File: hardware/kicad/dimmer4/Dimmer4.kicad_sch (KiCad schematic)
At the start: 41 parts, among them J100 Stapelstecker 2x20, J101 Kettenstecker, Buchse oben (S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, J102 Kettenstecker, Stift unten (S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, J103 Leistungsstecker, Buchse oben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, J104 Leistungsstecker, Stift unten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, J5 LED-Kanal 1, J6 LED-Kanal 2, J7 LED-Kanal 3, J8 LED-Kanal 4, Q1 NCE6050KA, Q10 IRFR5305, Q2 NCE6050KA, Q3 NCE6050KA, Q4 NCE6050KA, U100 STM32C011F6P6, U101 SN74LVC1G175, U102 SN74LVC2G00DCUR, U103 SN74LVC1G08

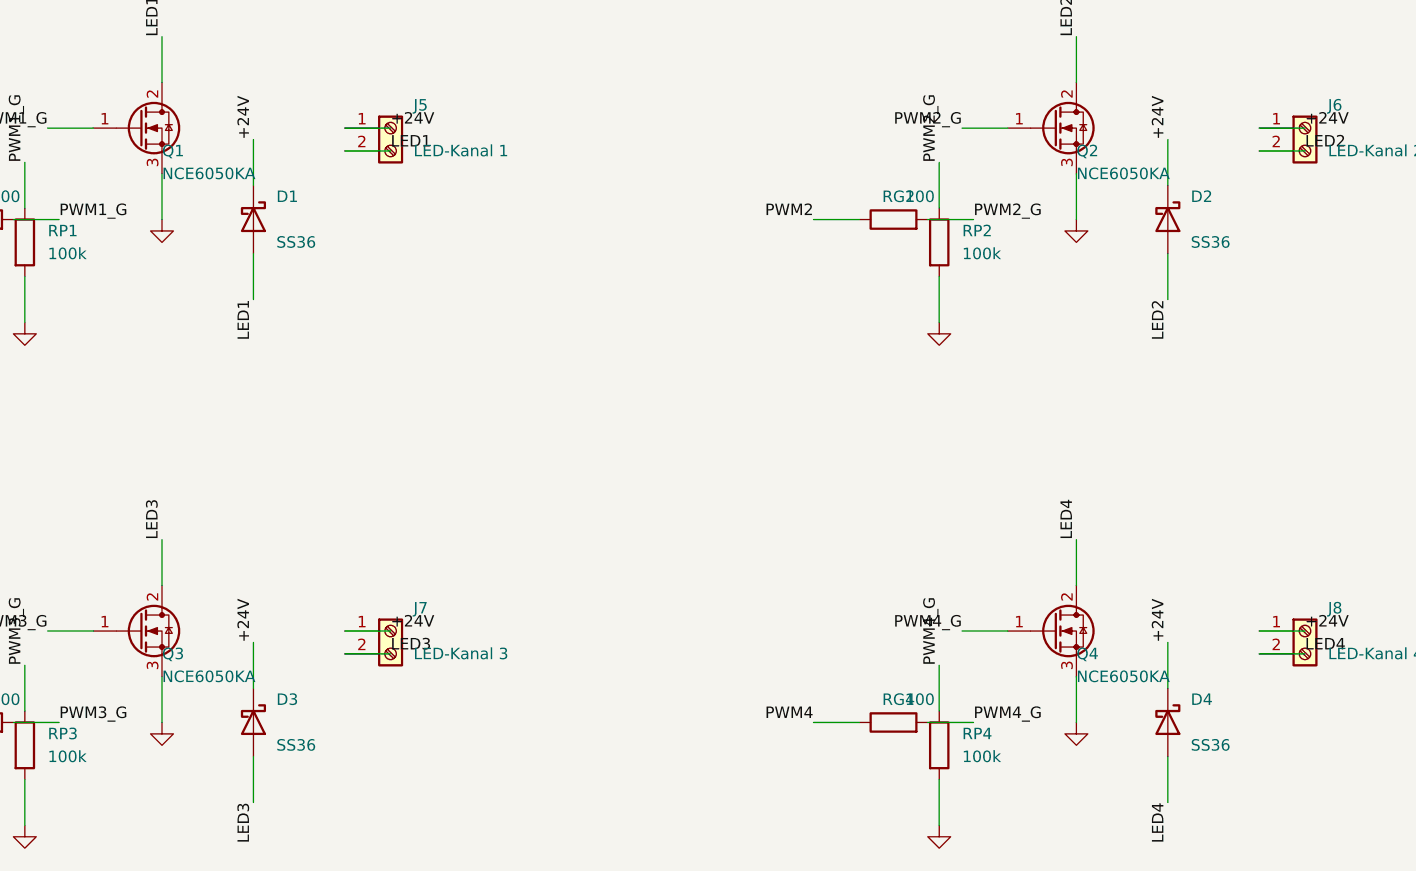
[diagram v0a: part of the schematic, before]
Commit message: Lager-Runde 2: NCE6020AK statt 6050KA, Basic-Widerstaende, Belege
JLCs zweiter Abgleich zeigte: NCE6050KA ausverkauft (3 Stueck Rest),
drei Widerstands-Matches auf Lager-0-Teile. Kanal-FET auf NCE6020AK
(C108639) umgestellt -- gleiches VGS(th)-Limit, Rechnung und ehrlicher
Vorbehalt in dimmermodul.py; Kennwiderstaende kriegen ihre Nummern
jetzt wertbasiert aus LCSC_KENN. Alle neuen Nummern an der
LCSC-Produktseite gesichtet (hardware/bauteile-dimmer.md, Nachtrag).
Dimmer-Schaltplaene regeneriert (ERC 0/0), 12 Suiten gruen.

Co-Authored-By: Claude Fable 5 <noreply@anthropic.com>
Claude-Session: https://claude.ai/code/session_01KDus95JJwCeRuwccgBWEi5
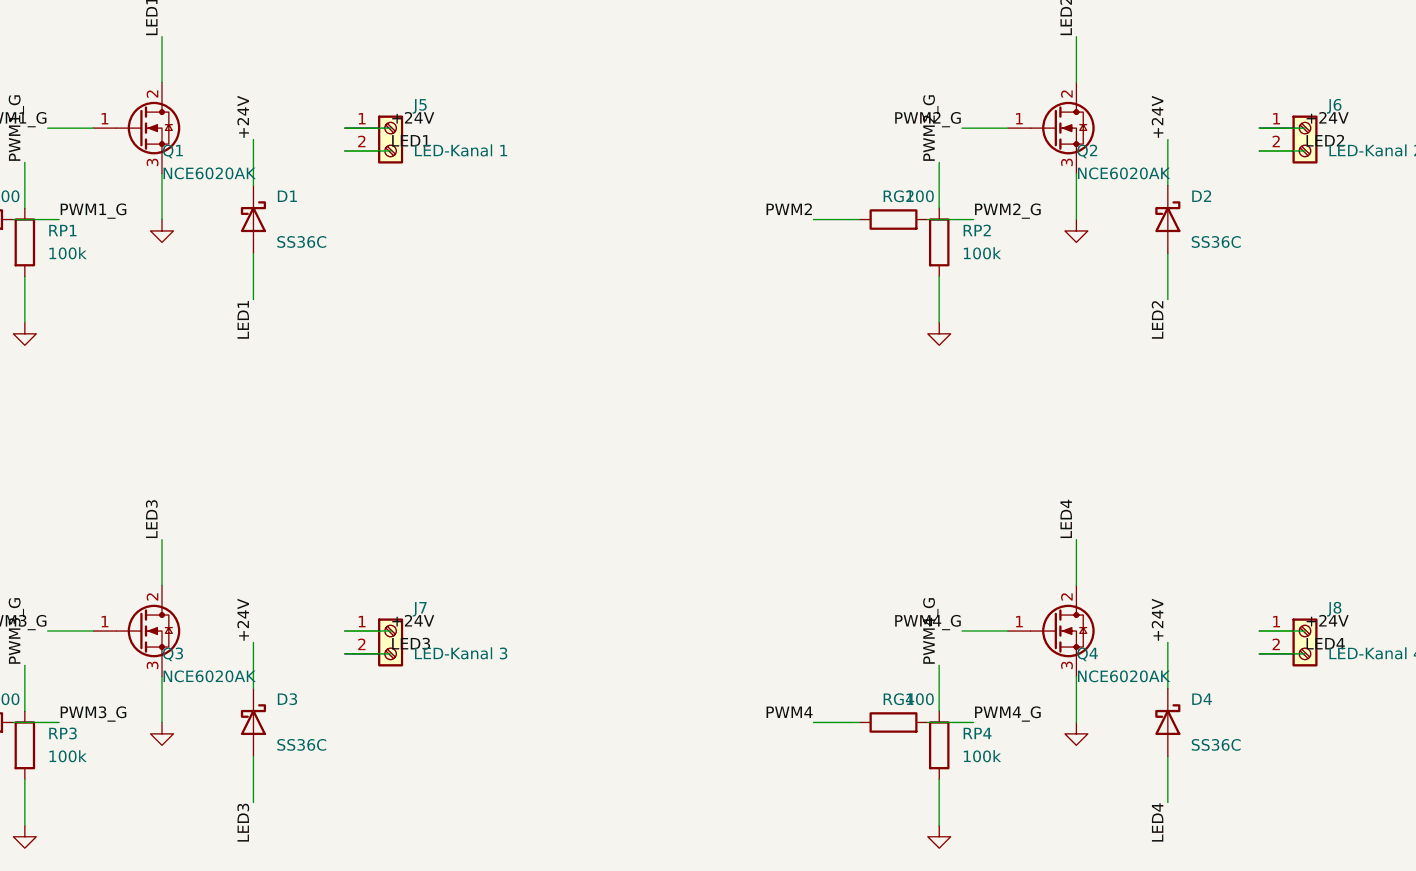
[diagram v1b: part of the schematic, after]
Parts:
- D1, D2, D3, D4: value SS36 -> SS36C
- Q1, Q2, Q3, Q4: value NCE6050KA -> NCE6020AK

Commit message: Dimmermodul v2: Versorgungszelle statt Q10-Strang, Gatter-Abblockung, v2-Scaffold
Ersetzt den alten Q10/R11/R12/D10/C12-Verpolschutzstrang durch
versorgung.bauen() (Task 3/5-Zelle, richtig gepolt) mit eigener
Einspeiseklemme J90; ergaenzt Abblockkondensatoren fuer U101/U102/U103
(bislang unversorgt) und die v2-Randpad-Kante (frei_durchreichen=True
+ randpads()) nach dem Motormodul-Muster.

PWM_PINS bleibt bewusst UNVERAENDERT: die vom Aufgabenbrief
vorgeschlagene Verlegung von Kanal 3/4 auf PA5/PA6 (Pin 12/13) ist
nicht moeglich, weil modulsockel.py diese Pins fuer JEDES Modul mit
mit_flipflop=True unbedingt auf NFAULT/IPROPI verdrahtet (verifiziert
am STM32C011-Symbol UND am Code) -- ueber die Kanal-1/2-Pins PA8/PA7
hinaus gibt es keinen einzigen freien Port-A-Pin. Volle Herleitung im
Docstring und in task-6-report.md.

ERC (severity-error) exit 0 fuer Dimmer1/3/4; Rot-Liste von
tests/run_all.py unveraendert (5 vorbestehende, unabhaengige
Fehlschlaege in sockelplatine.py/spec_sockel.py).

Co-Authored-By: Claude Fable 5 <noreply@anthropic.com>
Claude-Session: https://claude.ai/code/session_01KDus95JJwCeRuwccgBWEi5
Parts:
- removed C12: 220u, Capacitor_THT:CP_Radial_D8.0mm_P3.50mm, symbol Device:C_Polarized
- removed D10: SMCJ30A, Diode_SMD:D_SMC, symbol Device:D_Zener
- removed J100: Stapelstecker 2x20, Connector_PinHeader_2.54mm:PinHeader_2x20_P2.54mm_Vertical, symbol Connector_Generic:Conn_02x20_Odd_Even
- removed Q10: IRFR5305, Package_TO_SOT_SMD:TO-252-3_TabPin2, symbol Transistor_FET:Q_PMOS_GDS
- removed R11, R12: 10k, Resistor_SMD:R_0805_2012Metric_Pad1.20x1.40mm_HandSolder, symbol Device:R
- added C102, C103, C104: 100n, Capacitor_SMD:C_0805_2012Metric_Pad1.18x1.45mm_HandSolder, symbol Device:C
- added C90: 220u, Capacitor_THT:CP_Radial_D8.0mm_P3.50mm, symbol Device:C_Polarized
- added C91: 22u, Capacitor_SMD:C_0805_2012Metric_Pad1.18x1.45mm_HandSolder, symbol Device:C
- added D90: SMCJ30A, Diode_SMD:D_SMC, symbol Device:D_Zener
- added D91: SS36C, Diode_SMD:D_SMC, symbol Device:D_Schottky
- added J100: Stapelstecker links, Pico-Pins 1..20 (Buchse), Connector_PinSocket_2.54mm:PinSocket_1x20_P2.54mm_Vertical, symbol Connector_Generic:Conn_01x20
- added J105: Stapelstecker rechts, Pico-Pins 21..40 (Buchse), Connector_PinSocket_2.54mm:PinSocket_1x20_P2.54mm_Vertical, symbol Connector_Generic:Conn_01x20
- added J90: Versorgung Eingang, TerminalBlock_Phoenix:TerminalBlock_Phoenix_PT-1,5-2-3.5-H_1x02_P3.50mm_Horizontal, symbol Connector:Screw_Terminal_01x02
- added J95: Randpads GPIO, unbestueckt (THT-Loetpad), Connector_PinHeader_2.54mm:PinHeader_1x18_P2.54mm_Vertical, symbol Connector_Generic:Conn_01x18
- added J96: Randpads Versorgung: 2x 3V3 + 2x GND, unbestueckt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, Connector_PinHeader_2.54mm:PinHeader_1x04_P2.54mm_Vertical, symbol Connector_Generic:Conn_01x04
- added Q90: IRFR5305, Package_TO_SOT_SMD:TO-252-3_TabPin2, symbol Transistor_FET:Q_PMOS_GDS
- added R90, R91: 10k, Resistor_SMD:R_0805_2012Metric_Pad1.20x1.40mm_HandSolder, symbol Device:R
- added U90: K7805-1000R3, Converter_DCDC:Converter_DCDC_RECOM_R-78B-2.0_THT, symbol Converter_DCDC:R-78B5.0-2.0
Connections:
- net PWR24V is gone; now on net +24V: J103.1 (Pin_1), J103.3 (Pin_3), J104.1 (Pin_1), J104.3 (Pin_3)
- net +24V: now also C90.1, D90.1 (K), Q90.3 (S), R90.2, U90.1 (IN)
- net 3V3: now also C102.1, C102.2, C103.1, C103.2, C104.1, C104.2, C90.2, C91.2, D90.2 (A), J100.13 (Pin_13), J100.18 (Pin_18), J100.3 (Pin_3), J100.8 (Pin_8), J105.13 (Pin_13), J105.16 (Pin_16), J105.18 (Pin_18), J105.3 (Pin_3), J105.8 (Pin_8), J90.2 (Pin_2), J96.1 (Pin_1), J96.2 (Pin_2), J96.3 (Pin_3), J96.4 (Pin_4), R91.2, U90.2 (GND)
- net FLASH_MODE: now also J100.5 (Pin_5)
- net FLASH_RX: now also J100.2 (Pin_2)
- net FLASH_TX: now also J100.1 (Pin_1)
- net I2C_SCL: now also J100.7 (Pin_7)
- net I2C_SDA: now also J100.6 (Pin_6)
- net NOTAUS: now also J100.9 (Pin_9)
- net SEL_CLK: now also J100.10 (Pin_10)
- new net +5V_LOKAL: C91.1, D91.2 (A), U90.3 (OUT)
- new net GP10: J100.14 (Pin_14), J95.3 (Pin_3)
- new net GP11: J100.15 (Pin_15), J95.4 (Pin_4)
- new net GP12: J100.16 (Pin_16), J95.5 (Pin_5)
- new net GP13: J100.17 (Pin_17), J95.6 (Pin_6)
- new net GP14: J100.19 (Pin_19), J95.7 (Pin_7)
- new net GP15: J100.20 (Pin_20), J95.8 (Pin_8)
- new net GP16: J105.1 (Pin_1), J95.9 (Pin_9)
- new net GP17: J105.2 (Pin_2), J95.10 (Pin_10)
- new net GP18: J105.4 (Pin_4), J95.11 (Pin_11)
- new net GP19: J105.5 (Pin_5), J95.12 (Pin_12)
- new net GP20: J105.6 (Pin_6), J95.13 (Pin_13)
- new net GP21: J105.7 (Pin_7), J95.14 (Pin_14)
- new net GP22: J105.9 (Pin_9), J95.15 (Pin_15)
- new net GP26: J105.11 (Pin_11), J95.16 (Pin_16)
- new net GP27: J105.12 (Pin_12), J95.17 (Pin_17)
- new net GP28: J105.14 (Pin_14), J95.18 (Pin_18)
- new net GP8: J100.11 (Pin_11), J95.1 (Pin_1)
- new net GP9: J100.12 (Pin_12), J95.2 (Pin_2)
- new net PWR_IN: J90.1 (Pin_1), Q90.2 (D)
- new net Q90_GATE: Q90.1 (G), R90.1, R91.1
- new net VSYS: D91.1 (K), J105.19 (Pin_19)
- no-connect marks 25 -> 6

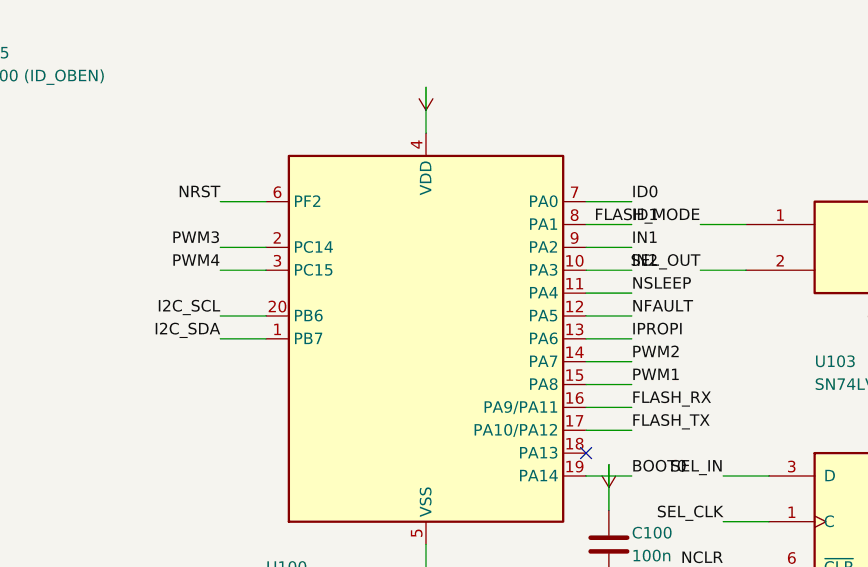
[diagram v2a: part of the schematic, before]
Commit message: Fix-Runde 1 zu Task 6: Motorsignale optional, PWM3/4 auf PA5/PA6
modulsockel.einbauen() verdrahtete PA2..PA6 (Pin 9-13) bisher
UNBEDINGT auf die DRV8876-Motorsignale (IN1/IN2/NSLEEP/NFAULT/IPROPI)
-- eine Altlast aus der Zeit mit nur einem Modultyp, die jedem Modul
ohne eigenen Motortreiber fuenf Port-A-Pins kostete. Neuer Parameter
motorsignale=False (Vorgabe): nur ein Modul mit motorsignale=True
(Motormodul) bekommt die feste Verdrahtung, jedes andere Modul
behandelt die fuenf Pins wie gewoehnliche freie GPIO (zusatz_pins oder
no_connect).

Motormodul fordert die Signale jetzt explizit an (motorsignale=True) --
Regressionsnachweis: generierte Netzliste vor/nach dem Umbau
byte-identisch (Schaltplan-Diff und Netlist-Export je UUID-/Datum-
normalisiert verglichen), ERC unveraendert 0 Fehler/2 Warnungen.

Dimmermodul: PWM3/4 ziehen von den schwach treibenden OSC32-Pins
PC14/PC15 auf PA5/PA6 (Pin 12/13) um -- damit haben jetzt alle vier
Kanaele Port-A-Pins mit Timer-Faehigkeit. tests/test_modulsockel.py
angepasst (Erwartungswert + drei neue Gegenproben fuer das neue
motorsignale-Verhalten, inkl. Kollisions-ValueError).

ERC (severity-error) exit 0 fuer Motormodul + Dimmer1/3/4; Rot-Liste
von tests/run_all.py unveraendert bei den 5 vorbestehenden,
unabhaengigen Fehlschlaegen.

Co-Authored-By: Claude Fable 5 <noreply@anthropic.com>
Claude-Session: https://claude.ai/code/session_01KDus95JJwCeRuwccgBWEi5
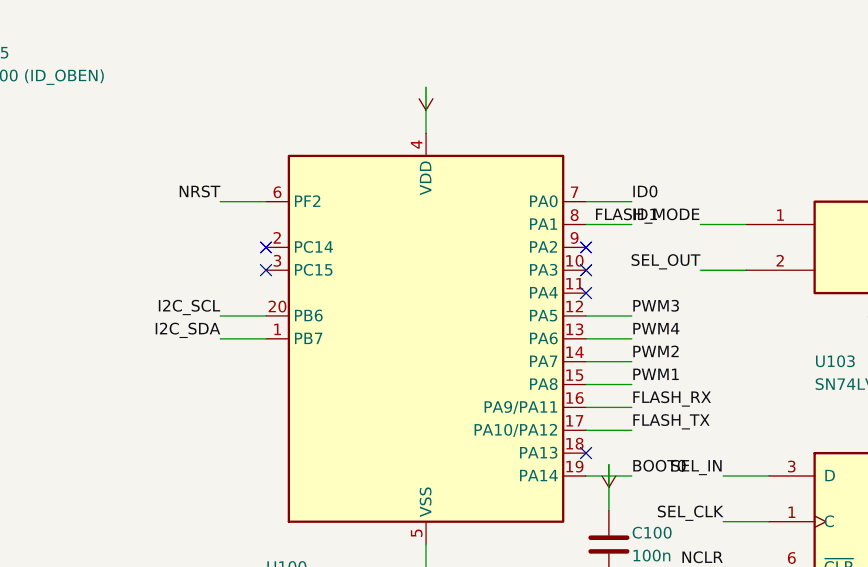
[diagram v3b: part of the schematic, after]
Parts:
- removed C102: 100n, Capacitor_SMD:C_0805_2012Metric_Pad1.18x1.45mm_HandSolder, symbol Device:C
- removed D4: SS36C, Diode_SMD:D_SMC, symbol Device:D_Schottky
- removed J8: LED-Kanal 4, TerminalBlock_Phoenix:TerminalBlock_Phoenix_PT-1,5-2-3.5-H_1x02_P3.50mm_Horizontal, symbol Connector:Screw_Terminal_01x02
- removed J95: Randpads GPIO, unbestueckt (THT-Loetpad), Connector_PinHeader_2.54mm:PinHeader_1x18_P2.54mm_Vertical, symbol Connector_Generic:Conn_01x18
- removed Q4: NCE6020AK, Package_TO_SOT_SMD:TO-252-3_TabPin2, symbol Transistor_FET:Q_NMOS_GDS
- removed RG4: 100, Resistor_SMD:R_0805_2012Metric_Pad1.20x1.40mm_HandSolder, symbol Device:R
- removed RP4: 100k, Resistor_SMD:R_0805_2012Metric_Pad1.20x1.40mm_HandSolder, symbol Device:R
- added C90: 220u, Capacitor_THT:CP_Radial_D8.0mm_P3.50mm, symbol Device:C_Polarized
- added J100: Stapelstecker links, Pico-Pins 1..20 (Buchse), Connector_PinSocket_2.54mm:PinSocket_1x20_P2.54mm_Vertical, symbol Connector_Generic:Conn_01x20
- added J101: Kettenstecker, Buchse oben (SMD), Connector_PinSocket_2.54mm:PinSocket_1x02_P2.54mm_Vertical_SMD_Pin1Left, symbol Connector_Generic:Conn_01x02
- added J102: Kettenstecker, Stift unten (SMD), Connector_PinHeader_2.54mm:PinHeader_1x02_P2.54mm_Vertical_SMD_Pin1Left, symbol Connector_Generic:Conn_01x02
- added J103: Leistungsstecker, Buchse oben (SMD), Connector_PinSocket_2.54mm:PinSocket_2x02_P2.54mm_Vertical_SMD, symbol Connector_Generic:Conn_02x02_Odd_Even
- added J105: Stapelstecker rechts, Pico-Pins 21..40 (Buchse), Connector_PinSocket_2.54mm:PinSocket_1x20_P2.54mm_Vertical, symbol Connector_Generic:Conn_01x20
- added R91: 10k, Resistor_SMD:R_0805_2012Metric_Pad1.20x1.40mm_HandSolder, symbol Device:R
- C100: renamed from J101; value Kettenstecker, Buchse oben (SMD) -> 100n; footprint Connector_PinSocket_2.54mm:PinSocket_1x02_P2.54mm_Vertical_SMD_Pin1Left -> Capacitor_SMD:C_0805_2012Metric_Pad1.18x1.45mm_HandSolder; symbol Connector_Generic:Conn_01x02 -> Device:C
- C101: renamed from J104; value Leistungsstecker, Stift unten (SMD) -> 1000n; footprint Connector_PinHeader_2.54mm:PinHeader_2x02_P2.54mm_Vertical_SMD -> Capacitor_SMD:C_0805_2012Metric_Pad1.18x1.45mm_HandSolder; symbol Connector_Generic:Conn_02x02_Odd_Even -> Device:C
- C102: renamed from R100; value Kennwiderstand (Modultyp) -> 100n; footprint Resistor_SMD:R_0805_2012Metric_Pad1.20x1.40mm_HandSolder -> Capacitor_SMD:C_0805_2012Metric_Pad1.18x1.45mm_HandSolder; symbol Device:R -> Device:C; LCSC (none) -> C49678
- C103: renamed from R105; value 10000 (ID_OBEN) -> 100n; footprint Resistor_SMD:R_0805_2012Metric_Pad1.20x1.40mm_HandSolder -> Capacitor_SMD:C_0805_2012Metric_Pad1.18x1.45mm_HandSolder; symbol Device:R -> Device:C; LCSC (none) -> C49678
- C104: renamed from R101; value Kennwiderstand (Modultyp) -> 100n; footprint Resistor_SMD:R_0805_2012Metric_Pad1.20x1.40mm_HandSolder -> Capacitor_SMD:C_0805_2012Metric_Pad1.18x1.45mm_HandSolder; symbol Device:R -> Device:C; LCSC (none) -> C49678
- C91: renamed from R90; value 10k -> 22u; footprint Resistor_SMD:R_0805_2012Metric_Pad1.20x1.40mm_HandSolder -> Capacitor_SMD:C_0805_2012Metric_Pad1.18x1.45mm_HandSolder; symbol Device:R -> Device:C
- D1: renamed from C91; value 22u -> SS36C; footprint Capacitor_SMD:C_0805_2012Metric_Pad1.18x1.45mm_HandSolder -> Diode_SMD:D_SMC; symbol Device:C -> Device:D_Schottky
- D90: renamed from J90; value Versorgung Eingang -> SMCJ30A; footprint TerminalBlock_Phoenix:TerminalBlock_Phoenix_PT-1,5-2-3.5-H_1x02_P3.50mm_Horizontal -> Diode_SMD:D_SMC; symbol Connector:Screw_Terminal_01x02 -> Device:D_Zener
- D91: renamed from R91; value 10k -> SS36C; footprint Resistor_SMD:R_0805_2012Metric_Pad1.20x1.40mm_HandSolder -> Diode_SMD:D_SMC; symbol Device:R -> Device:D_Schottky
- J104: renamed from J100; value Stapelstecker links, Pico-Pins 1..20 (Buchse) -> Leistungsstecker, Stift unten (SMD); footprint Connector_PinSocket_2.54mm:PinSocket_1x20_P2.54mm_Vertical -> Connector_PinHeader_2.54mm:PinHeader_2x02_P2.54mm_Vertical_SMD; symbol Connector_Generic:Conn_01x20 -> Connector_Generic:Conn_02x02_Odd_Even
- J5: renamed from D91; value SS36C -> LED-Kanal 1; footprint Diode_SMD:D_SMC -> TerminalBlock_Phoenix:TerminalBlock_Phoenix_PT-1,5-2-3.5-H_1x02_P3.50mm_Horizontal; symbol Device:D_Schottky -> Connector:Screw_Terminal_01x02
- J6: renamed from J5; value LED-Kanal 1 -> LED-Kanal 2
- J7: renamed from J6; value LED-Kanal 2 -> LED-Kanal 3
- J8: renamed from J7; value LED-Kanal 3 -> LED-Kanal 4
- J90: renamed from J96; value Randpads Versorgung: 2x 3V3 + 2x GND, unbestueckt (THT-Loetpad) -> Versorgung Eingang; footprint Connector_PinHeader_2.54mm:PinHeader_1x04_P2.54mm_Vertical -> TerminalBlock_Phoenix:TerminalBlock_Phoenix_PT-1,5-2-3.5-H_1x02_P3.50mm_Horizontal; symbol Connector_Generic:Conn_01x04 -> Connector:Screw_Terminal_01x02; now fitted
- J95: renamed from U103; value SN74LVC1G08 -> Randpads GPIO, unbestueckt (THT-Loetpad); footprint Package_TO_SOT_SMD:SOT-353_SC-70-5 -> Connector_PinHeader_2.54mm:PinHeader_1x18_P2.54mm_Vertical; symbol 74xGxx:74LVC1G08 -> Connector_Generic:Conn_01x18; now not fitted
- J96: renamed from R104; value 10000 (ID_OBEN) -> Randpads Versorgung: 2x 3V3 + 2x GND, unbestueckt (THT-Loetpad); footprint Resistor_SMD:R_0805_2012Metric_Pad1.20x1.40mm_HandSolder -> Connector_PinHeader_2.54mm:PinHeader_1x04_P2.54mm_Vertical; symbol Device:R -> Connector_Generic:Conn_01x04; now not fitted
- Q1: renamed from D90; value SMCJ30A -> NCE6020AK; footprint Diode_SMD:D_SMC -> Package_TO_SOT_SMD:TO-252-3_TabPin2; symbol Device:D_Zener -> Transistor_FET:Q_NMOS_GDS
- Q90: renamed from C103; value 100n -> IRFR5305; footprint Capacitor_SMD:C_0805_2012Metric_Pad1.18x1.45mm_HandSolder -> Package_TO_SOT_SMD:TO-252-3_TabPin2; symbol Device:C -> Transistor_FET:Q_PMOS_GDS; LCSC C49678 -> (none)
- R100, R101: renamed from U102; value SN74LVC2G00DCUR -> Kennwiderstand (Modultyp); footprint Package_SO:VSSOP-8_2.3x2mm_P0.5mm -> Resistor_SMD:R_0805_2012Metric_Pad1.20x1.40mm_HandSolder; symbol 74xGxx:74LVC2G00 -> Device:R
- R102: renamed from J103; value Leistungsstecker, Buchse oben (SMD) -> 100k; footprint Connector_PinSocket_2.54mm:PinSocket_2x02_P2.54mm_Vertical_SMD -> Resistor_SMD:R_0805_2012Metric_Pad1.20x1.40mm_HandSolder; symbol Connector_Generic:Conn_02x02_Odd_Even -> Device:R
- R104: renamed from C101; value 1000n -> 10000 (ID_OBEN); footprint Capacitor_SMD:C_0805_2012Metric_Pad1.18x1.45mm_HandSolder -> Resistor_SMD:R_0805_2012Metric_Pad1.20x1.40mm_HandSolder; symbol Device:C -> Device:R
- R105: renamed from U102; value SN74LVC2G00DCUR -> 10000 (ID_OBEN); footprint Package_SO:VSSOP-8_2.3x2mm_P0.5mm -> Resistor_SMD:R_0805_2012Metric_Pad1.20x1.40mm_HandSolder; symbol 74xGxx:74LVC2G00 -> Device:R
- R90: renamed from C104; value 100n -> 10k; footprint Capacitor_SMD:C_0805_2012Metric_Pad1.18x1.45mm_HandSolder -> Resistor_SMD:R_0805_2012Metric_Pad1.20x1.40mm_HandSolder; symbol Device:C -> Device:R; LCSC C49678 -> (none)
- RG1: renamed from C90; value 220u -> 100; footprint Capacitor_THT:CP_Radial_D8.0mm_P3.50mm -> Resistor_SMD:R_0805_2012Metric_Pad1.20x1.40mm_HandSolder; symbol Device:C_Polarized -> Device:R
- RP1: renamed from U90; value K7805-1000R3 -> 100k; footprint Converter_DCDC:Converter_DCDC_RECOM_R-78B-2.0_THT -> Resistor_SMD:R_0805_2012Metric_Pad1.20x1.40mm_HandSolder; symbol Converter_DCDC:R-78B5.0-2.0 -> Device:R
- U100: renamed from J105; value Stapelstecker rechts, Pico-Pins 21..40 (Buchse) -> STM32C011F6P6; footprint Connector_PinSocket_2.54mm:PinSocket_1x20_P2.54mm_Vertical -> Package_SO:TSSOP-20_4.4x6.5mm_P0.65mm; symbol Connector_Generic:Conn_01x20 -> MCU_ST_STM32C0:STM32C011F6Px
- U101: renamed from J102; value Kettenstecker, Stift unten (SMD) -> SN74LVC1G175; footprint Connector_PinHeader_2.54mm:PinHeader_1x02_P2.54mm_Vertical_SMD_Pin1Left -> Package_TO_SOT_SMD:SOT-363_SC-70-6; symbol Connector_Generic:Conn_01x02 -> 74xGxx:74LVC1G175
- U102: renamed from U100; value STM32C011F6P6 -> SN74LVC2G00DCUR; footprint Package_SO:TSSOP-20_4.4x6.5mm_P0.65mm -> Package_SO:VSSOP-8_2.3x2mm_P0.5mm; symbol MCU_ST_STM32C0:STM32C011F6Px -> 74xGxx:74LVC2G00
- U102: renamed from C100; value 100n -> SN74LVC2G00DCUR; footprint Capacitor_SMD:C_0805_2012Metric_Pad1.18x1.45mm_HandSolder -> Package_SO:VSSOP-8_2.3x2mm_P0.5mm; symbol Device:C -> 74xGxx:74LVC2G00
- U102: renamed from U101; value SN74LVC1G175 -> SN74LVC2G00DCUR; footprint Package_TO_SOT_SMD:SOT-363_SC-70-6 -> Package_SO:VSSOP-8_2.3x2mm_P0.5mm; symbol 74xGxx:74LVC1G175 -> 74xGxx:74LVC2G00
- U103: renamed from R102; value 100k -> SN74LVC1G08; footprint Resistor_SMD:R_0805_2012Metric_Pad1.20x1.40mm_HandSolder -> Package_TO_SOT_SMD:SOT-353_SC-70-5; symbol Device:R -> 74xGxx:74LVC1G08
- U90: renamed from Q90; value IRFR5305 -> K7805-1000R3; footprint Package_TO_SOT_SMD:TO-252-3_TabPin2 -> Converter_DCDC:Converter_DCDC_RECOM_R-78B-2.0_THT; symbol Transistor_FET:Q_PMOS_GDS -> Converter_DCDC:R-78B5.0-2.0
- renumbered D1 to D2, D2 to D3, D3 to D4, Q1 to Q2, Q2 to Q3, Q3 to Q4, RG1 to RG2, RG2 to RG3, RG3 to RG4, RP1 to RP2, RP2 to RP3, RP3 to RP4
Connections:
- net +24V: now also D1.1 (K), D90.1 (K), J104.1 (Pin_1), J104.3 (Pin_3), J5.1 (Pin_1), Q90.3 (S), R90.2, U90.1 (IN), C90.1, J103.1 (Pin_1), J103.3 (Pin_3); no longer C101.1 (Pin_1), C101.3 (Pin_3), C91.2, Q1.1 (K), R102.1 (Pin_1), R102.3 (Pin_3), RG1.1, RP1.1 (IN), U90.3 (S)
- net +5V_LOKAL: now also C91.1, D91.2 (A), U90.3 (OUT); no longer D1.1, J5.2 (A), RP1.3 (OUT)
- net 3V3: now also C100.1, C102.1, C103.2, C104.1, C91.2, J104.2 (Pin_2), J104.4 (Pin_4), J96.2 (Pin_2), J96.3 (Pin_3), J96.4 (Pin_4), Q1.3 (S), R100.2, R101.2, R102.1, R104.1, R105.1, U100.4 (VDD), U100.5 (VSS), U101.5 (VCC), U102.4 (GND), U102.8 (VCC), U103.3 (GND), U103.5 (VCC), U90.2 (GND), C90.2, J100.13 (Pin_13), J100.18 (Pin_18), J100.3 (Pin_3), J100.8 (Pin_8), J101.2 (Pin_2), J102.2 (Pin_2), J103.2 (Pin_2), J103.4 (Pin_4), J105.13 (Pin_13), J105.16 (Pin_16), J105.18 (Pin_18), J105.3 (Pin_3), J105.8 (Pin_8), R91.2; no longer C101.4 (Pin_4), D1.2, D91.2, J104.13 (Pin_13), J104.18 (Pin_18), J104.3 (Pin_3), J104.8 (Pin_8), J90.1 (Pin_1), J90.3 (Pin_3), J90.4 (Pin_4), J95.3 (GND), J95.5 (VCC), Q1.2 (A), Q90.1, Q90.2, R101.4 (GND), R101.8 (VCC), R102.2 (Pin_2), R102.4 (Pin_4), R104.2, R90.1, R90.2, RG1.2, U100.13 (Pin_13), U100.16 (Pin_16), U100.18 (Pin_18), U100.3 (Pin_3), U100.8 (Pin_8), U102.1, U102.2, U102.2 (GND), U102.4 (VDD), U102.5 (VCC), U102.5 (VSS), U103.1
- net BOOT0: now also U100.19 (PA14), U103.4; no longer J95.4, U102.19 (PA14)
- net FLASH_MODE: now also U102.5, U103.1, J100.5 (Pin_5); no longer J104.5 (Pin_5), J95.1, R105.5
- net FLASH_RX: now also U100.16 (PA9/PA11), J100.2 (Pin_2); no longer J104.2 (Pin_2), U102.16 (PA9/PA11)
- net FLASH_TX: now also U100.17 (PA10/PA12), J100.1 (Pin_1); no longer J104.1 (Pin_1), U102.17 (PA10/PA12)
- net GP10: now also J95.3 (Pin_3), J100.14 (Pin_14); no longer J104.14 (Pin_14)
- net GP11: now also J95.4 (Pin_4), J100.15 (Pin_15); no longer J104.15 (Pin_15)
- net GP12: now also J95.5 (Pin_5), J100.16 (Pin_16); no longer J104.16 (Pin_16)
- net GP13: now also J95.6 (Pin_6), J100.17 (Pin_17); no longer J104.17 (Pin_17)
- net GP14: now also J95.7 (Pin_7), J100.19 (Pin_19); no longer J104.19 (Pin_19)
- net GP15: now also J95.8 (Pin_8), J100.20 (Pin_20); no longer J104.20 (Pin_20)
- net GP16: now also J95.9 (Pin_9), J105.1 (Pin_1); no longer U100.1 (Pin_1)
- net GP17: now also J95.10 (Pin_10), J105.2 (Pin_2); no longer U100.2 (Pin_2)
- net GP18: now also J95.11 (Pin_11), J105.4 (Pin_4); no longer U100.4 (Pin_4)
- net GP19: now also J95.12 (Pin_12), J105.5 (Pin_5); no longer U100.5 (Pin_5)
- net GP20: now also J95.13 (Pin_13), J105.6 (Pin_6); no longer U100.6 (Pin_6)
- net GP21: now also J95.14 (Pin_14), J105.7 (Pin_7); no longer U100.7 (Pin_7)
- net GP22: now also J95.15 (Pin_15), J105.9 (Pin_9); no longer U100.9 (Pin_9)
- net GP26: now also J95.16 (Pin_16), J105.11 (Pin_11); no longer U100.11 (Pin_11)
- net GP27: now also J95.17 (Pin_17), J105.12 (Pin_12); no longer U100.12 (Pin_12)
- net GP28: now also J95.18 (Pin_18), J105.14 (Pin_14); no longer U100.14 (Pin_14)
- net GP8: now also J95.1 (Pin_1), J100.11 (Pin_11); no longer J104.11 (Pin_11)
- net GP9: now also J95.2 (Pin_2), J100.12 (Pin_12); no longer J104.12 (Pin_12)
- net I2C_SCL: now also U100.20 (PB6), J100.7 (Pin_7); no longer J104.7 (Pin_7), U102.20 (PB6)
- net I2C_SDA: now also U100.1 (PB7), J100.6 (Pin_6); no longer J104.6 (Pin_6), U102.1 (PB7)
- net ID0: now also R100.1, R104.2, U100.7 (PA0); no longer C102.1, J96.2, U102.7 (PA0)
- net ID1: now also R101.1, R105.2, U100.8 (PA1); no longer C103.2, C104.1, U102.8 (PA1)
- net LED1: now also D1.2 (A), J5.2 (Pin_2), Q1.2 (D); no longer D2.2 (A), J6.2 (Pin_2), Q2.2 (D)
- net LED2: now also D2.2 (A), J6.2 (Pin_2), Q2.2 (D); no longer D3.2 (A), J7.2 (Pin_2), Q3.2 (D)
- net LED3: now also D3.2 (A), J7.2 (Pin_2), Q3.2 (D); no longer D4.2 (A), J8.2 (Pin_2), Q4.2 (D)
- net LED4: now also D4.2 (A), J8.2 (Pin_2), Q4.2 (D)
- net NCLR: now also C101.1, R102.2, U101.6 (~{CLR}); no longer R104.1, U102.6 (~{CLR}), U103.2
- net NOTAUS: now also J100.9 (Pin_9); no longer J104.9 (Pin_9)
- net NQ: now also U102.6, U102.7; no longer R100.7, R105.6
- net NRST: now also U100.6 (PF2), U102.3; no longer R105.3, U102.6 (PF2)
- net PWM1: now also RG1.1, U100.15 (PA8); no longer RG2.1, U102.15 (PA8)
- net PWM1_G: now also Q1.1 (G), RG1.2, RP1.1; no longer Q2.1 (G), RG2.2, RP2.1
- net PWM2: now also RG2.1, U100.14 (PA7); no longer RG3.1, U102.14 (PA7)
- net PWM2_G: now also Q2.1 (G), RG2.2, RP2.1; no longer Q3.1 (G), RG3.2, RP3.1
- net PWM3: now also RG3.1, U100.12 (PA5); no longer RG4.1, U102.2 (PC14)
- net PWM3_G: now also Q3.1 (G), RG3.2, RP3.1; no longer Q4.1 (G), RG4.2, RP4.1
- net PWM4: now also RG4.1, U100.13 (PA6); no longer U102.3 (PC15)
- net PWM4_G: now also Q4.1 (G), RG4.2, RP4.1
- net PWR_IN: now also J90.1 (Pin_1), Q90.2 (D); no longer D90.1 (Pin_1), U90.2 (D)
- net Q90_GATE: now also Q90.1 (G), R90.1, R91.1; no longer C91.1, D91.1, U90.1 (G)
- net SEL_CLK: now also U101.1 (C), J100.10 (Pin_10); no longer J104.10 (Pin_10), U102.1 (C)
- net SEL_IN: now also U101.3 (D), J101.1 (Pin_1); no longer C100.1 (Pin_1), U102.3 (D)
- net SEL_OUT: now also U101.4 (Q), U102.1, U102.2, U103.2, J102.1 (Pin_1); no longer J95.2, R100.1, R100.2, U101.1 (Pin_1), U102.4 (Q)
- net VSYS: now also D91.1 (K), J105.19 (Pin_19); no longer J5.1 (K), U100.19 (Pin_19)
- removed net IN1: U102.9 (PA2)
- removed net IN2: U102.10 (PA3)
- removed net IPROPI: U102.13 (PA6)
- removed net NFAULT: U102.12 (PA5)
- removed net NSLEEP: U102.11 (PA4)
- no-connect marks 6 -> 11
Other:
- moved on the sheet: D2, D3, D4, J6, J7, J8, Q2, Q3, Q4, RG2, RG3, RG4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

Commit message: Aufgabe 8b: Vorverdrahtung fuer zwei nachweislich unverlegbare Netze
Erste Wuerfelserie (11 gueltige Wuerfe ueber Dimmer1/3/4) zeigte zwei
Verbindungen, die der Router systematisch liegen liess:

  /SEL_OUT  J102-1 <-> Nest-Via        8 von 11 Wuerfen offen
  3V3       R102-1 <-> C100-1/U100-4   7 von 11 offen

Beide sind jetzt in spec_dimmer_basis.EIGENE_PRE_TRACKS vorverdrahtet.
Die Koordinaten sind nicht geraten, sondern aus dem fertig verlegten
Motormodul (Commit 8c6c52a, DRC 0/0) uebernommen: das Nest ist dort
bauteilgleich und dichter belegt als im Dimmer, sein Kupfer ist also
der billigste vorhandene Beweis, dass die Gasse traegt. Wirkung ueber
je fuenf neue Wuerfe: offene Posten von 2,9 auf 1,4 im Mittel.

Zwei Nebenfixe:

* autoroute.ZEITGRENZE (vorher hart 420 s) auf 2700 s. Nicht weil
  dieser Auftrag sie gerissen haette -- gemessen brauchten die
  Dimmer-Wuerfe 20..380 s --, sondern weil Aufgabe 7c sie am
  Motormodul gerissen hat und sie dort gute Arbeit weggeworfen statt
  einen Fehler gemeldet hat. Der GUI-Haenger, gegen den die 420 s
  urspruenglich standen, ist seit FREEROUTING__GUI__ENABLED=false
  ausgeschlossen; Begruendung im Kommentar neu gefasst.

* J95/J96 tragen in allen drei .kicad_sch jetzt den projekteigenen
  Footprint Randpads:Randpad_Reihe_1x18/1x04 statt des KiCad-
  Stiftleisten-Standards. build.py hat das bisher jeden Lauf gemeldet
  ("Schaltplan will ..., Beschreibung ..."); gebaut hat es korrekt,
  die BOM-Seite zeigte aber den falschen Footprint. Offener Punkt aus
  Aufgabe 8a, Abschnitt 10.

Co-Authored-By: Claude Fable 5 <noreply@anthropic.com>
Claude-Session: https://claude.ai/code/session_01KDus95JJwCeRuwccgBWEi5
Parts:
- J95: footprint Connector_PinHeader_2.54mm:PinHeader_1x18_P2.54mm_Vertical -> Randpads:Randpad_Reihe_1x18
- J96: footprint Connector_PinHeader_2.54mm:PinHeader_1x04_P2.54mm_Vertical -> Randpads:Randpad_Reihe_1x04
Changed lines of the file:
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@@
 			)
 		)
-		(property "Footprint" "Connector_PinHeader_2.54mm:PinHeader_1x18_P2.54mm_Vertical"
+		(property "Footprint" "Randpads:Randpad_Reihe_1x18"
 			(at 0 -101.6 0)
 			(show_name no)
@@
 			)
 		)
-		(property "Footprint" "Connector_PinHeader_2.54mm:PinHeader_1x04_P2.54mm_Vertical"
+		(property "Footprint" "Randpads:Randpad_Reihe_1x04"
 			(at 30.48 -101.6 0)
 			(show_name no)
